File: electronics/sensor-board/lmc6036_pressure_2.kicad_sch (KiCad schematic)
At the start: 21 parts

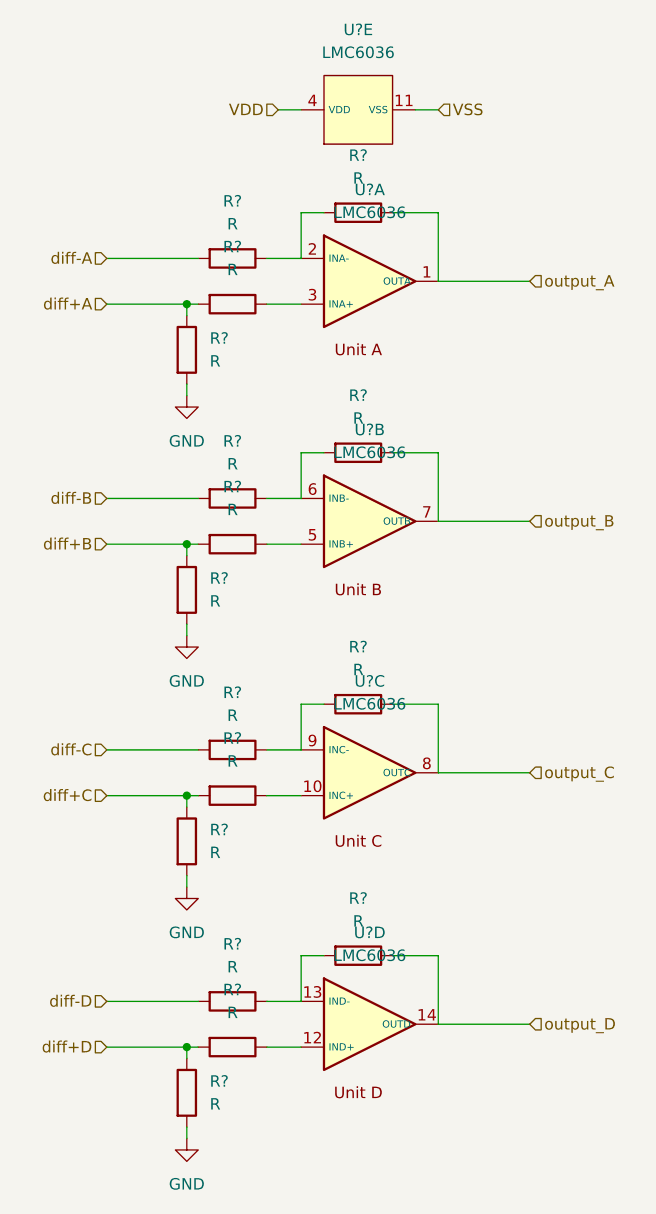
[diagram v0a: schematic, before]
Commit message: sensor-board edits
Finalized pressure and flow sensor circuits.
Reorganized schematics
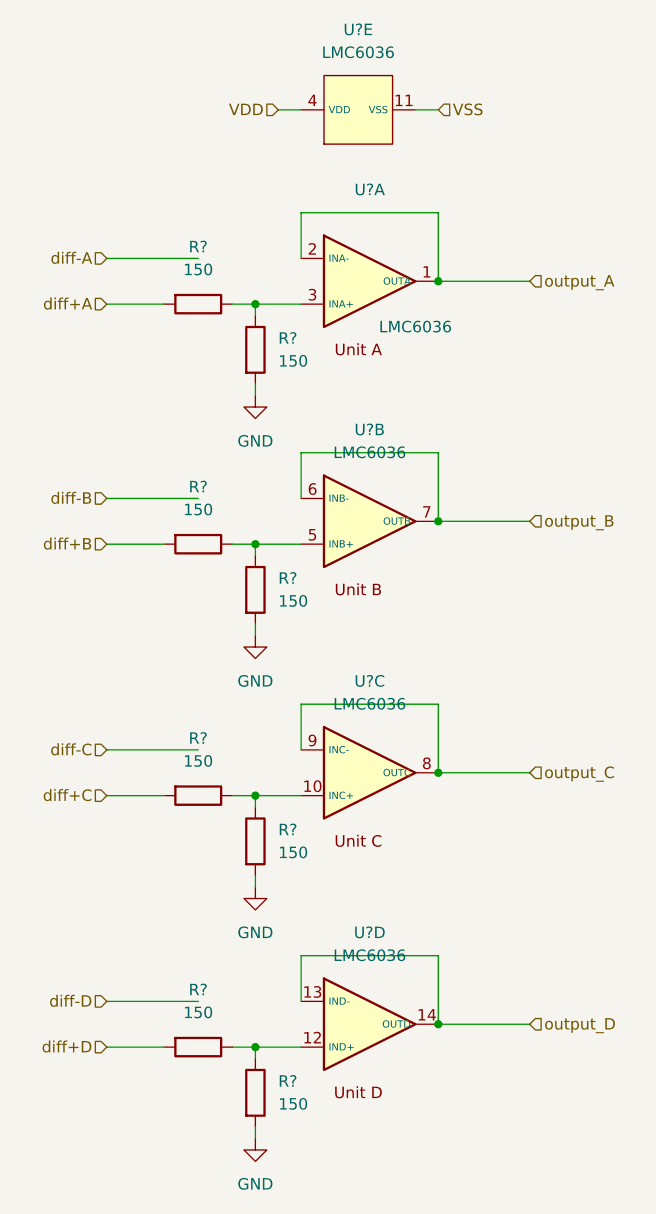
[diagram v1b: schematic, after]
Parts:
- removed R? (x16): R, symbol Device:R
- removed U? (x5): LMC6036, LMC6036:SOP65P640X120-14N, symbol LMC6036_custom:LMC6036
- added R? (x8): 150, symbol Device:R
- added U? (x5): LMC6036, LMC6036:SOP65P640X120-14N, symbol LMC6036_custom:LMC6036
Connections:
- net GND: now also R?.2, R?.2, R?.2, R?.2
- net VDD: now also U?.4 (VDD)
- net VSS: now also U?.11 (VSS)
- net diff+A: now also R?.2
- net diff+B: now also R?.2
- net diff+C: now also R?.2
- net diff+D: now also R?.2
- net output_A: now also U?.1 (OUTA), U?.2 (INA-)
- net output_B: now also U?.6 (INB-), U?.7 (OUTB)
- net output_C: now also U?.8 (OUTC), U?.9 (INC-)
- net output_D: now also U?.13 (IND-), U?.14 (OUTD)
- new net: R?.1, R?.1, U?.10 (INC+)
- new net: R?.1, R?.1, U?.3 (INA+)
- new net: R?.1, R?.1, U?.12 (IND+)
- new net: R?.1, R?.1, U?.5 (INB+)

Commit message: work on sensor-board
added MCP960 footprint
finished MCP960 array schematic
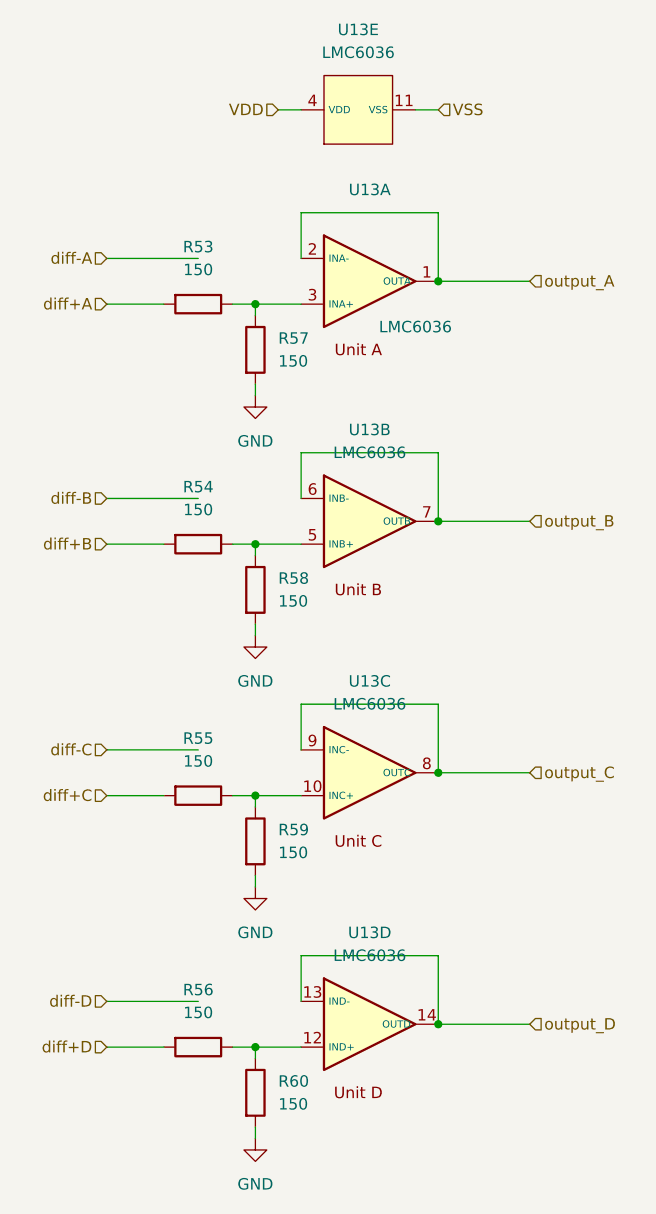
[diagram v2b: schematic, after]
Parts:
- R53, R54, R55, R56, R57, R58, R59, R60: renamed from R?; footprint (none) -> Resistor_SMD:R_0603_1608Metric
- gave numbers to parts that had none: 1
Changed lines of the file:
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@@
   (symbol (lib_id "power:GND") (at 142.24 76.2 0) (unit 1)
     (in_bom yes) (on_board yes) (fields_autoplaced)
-    (property "Reference" "#PWR?" (id 0) (at 142.24 82.55 0)
+    (property "Reference" "#PWR0181" (id 0) (at 142.24 82.55 0)
       (effects (font (size 1.27 1.27)) hide)
     )
@@
   (symbol (lib_id "power:GND") (at 142.24 102.87 0) (unit 1)
     (in_bom yes) (on_board yes) (fields_autoplaced)
-    (property "Reference" "#PWR?" (id 0) (at 142.24 109.22 0)
+    (property "Reference" "#PWR0183" (id 0) (at 142.24 109.22 0)
       (effects (font (size 1.27 1.27)) hide)
     )
@@
   (symbol (lib_id "power:GND") (at 142.24 130.81 0) (unit 1)
     (in_bom yes) (on_board yes) (fields_autoplaced)
-    (property "Reference" "#PWR?" (id 0) (at 142.24 137.16 0)
+    (property "Reference" "#PWR0182" (id 0) (at 142.24 137.16 0)
       (effects (font (size 1.27 1.27)) hide)
     )
@@
   (symbol (lib_id "power:GND") (at 142.24 158.75 0) (unit 1)
     (in_bom yes) (on_board yes) (fields_autoplaced)
-    (property "Reference" "#PWR?" (id 0) (at 142.24 165.1 0)
+    (property "Reference" "#PWR0184" (id 0) (at 142.24 165.1 0)
       (effects (font (size 1.27 1.27)) hide)
     )
@@
   (symbol (lib_id "Device:R") (at 135.89 66.04 270) (unit 1)
     (in_bom yes) (on_board yes) (fields_autoplaced)
-    (property "Reference" "R?" (id 0) (at 135.89 59.69 90))
+    (property "Reference" "R53" (id 0) (at 135.89 59.69 90))
     (property "Value" "150" (id 1) (at 135.89 62.23 90))
-    (property "Footprint" "" (id 2) (at 135.89 64.262 90)
+    (property "Footprint" "Resistor_SMD:R_0603_1608Metric" (id 2) (at 135.89 64.262 90)
       (effects (font (size 1.27 1.27)) hide)
     )
@@
   (symbol (lib_id "Device:R") (at 135.89 92.71 270) (unit 1)
     (in_bom yes) (on_board yes) (fields_autoplaced)
-    (property "Reference" "R?" (id 0) (at 135.89 86.36 90))
+    (property "Reference" "R54" (id 0) (at 135.89 86.36 90))
     (property "Value" "150" (id 1) (at 135.89 88.9 90))
-    (property "Footprint" "" (id 2) (at 135.89 90.932 90)
+    (property "Footprint" "Resistor_SMD:R_0603_1608Metric" (id 2) (at 135.89 90.932 90)
       (effects (font (size 1.27 1.27)) hide)
     )
@@
   (symbol (lib_id "Device:R") (at 135.89 120.65 270) (unit 1)
     (in_bom yes) (on_board yes) (fields_autoplaced)
-    (property "Reference" "R?" (id 0) (at 135.89 114.3 90))
+    (property "Reference" "R55" (id 0) (at 135.89 114.3 90))
     (property "Value" "150" (id 1) (at 135.89 116.84 90))
-    (property "Footprint" "" (id 2) (at 135.89 118.872 90)
+    (property "Footprint" "Resistor_SMD:R_0603_1608Metric" (id 2) (at 135.89 118.872 90)
       (effects (font (size 1.27 1.27)) hide)
     )
@@
   (symbol (lib_id "Device:R") (at 135.89 148.59 270) (unit 1)
     (in_bom yes) (on_board yes) (fields_autoplaced)
-    (property "Reference" "R?" (id 0) (at 135.89 142.24 90))
+    (property "Reference" "R56" (id 0) (at 135.89 142.24 90))
     (property "Value" "150" (id 1) (at 135.89 144.78 90))
-    (property "Footprint" "" (id 2) (at 135.89 146.812 90)
+    (property "Footprint" "Resistor_SMD:R_0603_1608Metric" (id 2) (at 135.89 146.812 90)
       (effects (font (size 1.27 1.27)) hide)
     )
@@
   (symbol (lib_id "Device:R") (at 142.24 71.12 0) (unit 1)
     (in_bom yes) (on_board yes) (fields_autoplaced)
-    (property "Reference" "R?" (id 0) (at 144.78 69.8499 0)
+    (property "Reference" "R57" (id 0) (at 144.78 69.8499 0)
       (effects (font (size 1.27 1.27)) (justify left))
     )
@@
       (effects (font (size 1.27 1.27)) (justify left))
     )
-    (property "Footprint" "" (id 2) (at 140.462 71.12 90)
+    (property "Footprint" "Resistor_SMD:R_0603_1608Metric" (id 2) (at 140.462 71.12 90)
       (effects (font (size 1.27 1.27)) hide)
     )
@@
   (symbol (lib_id "Device:R") (at 142.24 97.79 0) (unit 1)
     (in_bom yes) (on_board yes) (fields_autoplaced)
-    (property "Reference" "R?" (id 0) (at 144.78 96.5199 0)
+    (property "Reference" "R58" (id 0) (at 144.78 96.5199 0)
       (effects (font (size 1.27 1.27)) (justify left))
     )
@@
       (effects (font (size 1.27 1.27)) (justify left))
     )
-    (property "Footprint" "" (id 2) (at 140.462 97.79 90)
+    (property "Footprint" "Resistor_SMD:R_0603_1608Metric" (id 2) (at 140.462 97.79 90)
       (effects (font (size 1.27 1.27)) hide)
     )
@@
   (symbol (lib_id "Device:R") (at 142.24 125.73 0) (unit 1)
     (in_bom yes) (on_board yes) (fields_autoplaced)
-    (property "Reference" "R?" (id 0) (at 144.78 124.4599 0)
+    (property "Reference" "R59" (id 0) (at 144.78 124.4599 0)
       (effects (font (size 1.27 1.27)) (justify left))
     )
@@
       (effects (font (size 1.27 1.27)) (justify left))
     )
-    (property "Footprint" "" (id 2) (at 140.462 125.73 90)
+    (property "Footprint" "Resistor_SMD:R_0603_1608Metric" (id 2) (at 140.462 125.73 90)
       (effects (font (size 1.27 1.27)) hide)
     )
@@
   (symbol (lib_id "Device:R") (at 142.24 153.67 0) (unit 1)
     (in_bom yes) (on_board yes) (fields_autoplaced)
-    (property "Reference" "R?" (id 0) (at 144.78 152.3999 0)
+    (property "Reference" "R60" (id 0) (at 144.78 152.3999 0)
       (effects (font (size 1.27 1.27)) (justify left))
     )
@@
       (effects (font (size 1.27 1.27)) (justify left))
     )
-    (property "Footprint" "" (id 2) (at 140.462 153.67 90)
+    (property "Footprint" "Resistor_SMD:R_0603_1608Metric" (id 2) (at 140.462 153.67 90)
       (effects (font (size 1.27 1.27)) hide)
     )
@@
   (symbol (lib_id "LMC6036_custom:LMC6036") (at 153.67 44.45 90) (unit 5)
     (in_bom yes) (on_board yes) (fields_autoplaced)
-    (property "Reference" "U?" (id 0) (at 153.67 35.56 90))
+    (property "Reference" "U13" (id 0) (at 153.67 35.56 90))
     (property "Value" "LMC6036" (id 1) (at 153.67 38.1 90))
     (property "Footprint" "LMC6036:SOP65P640X120-14N" (id 2) (at 153.67 42.545 0)
@@
   (symbol (lib_id "LMC6036_custom:LMC6036") (at 153.67 63.5 0) (unit 1)
     (in_bom yes) (on_board yes)
-    (property "Reference" "U?" (id 0) (at 154.94 53.34 0))
+    (property "Reference" "U13" (id 0) (at 154.94 53.34 0))
     (property "Value" "LMC6036" (id 1) (at 160.02 68.58 0))
     (property "Footprint" "LMC6036:SOP65P640X120-14N" (id 2) (at 155.575 63.5 0)
@@
   (symbol (lib_id "LMC6036_custom:LMC6036") (at 153.67 90.17 0) (unit 2)
     (in_bom yes) (on_board yes) (fields_autoplaced)
-    (property "Reference" "U?" (id 0) (at 154.94 80.01 0))
+    (property "Reference" "U13" (id 0) (at 154.94 80.01 0))
     (property "Value" "LMC6036" (id 1) (at 154.94 82.55 0))
     (property "Footprint" "LMC6036:SOP65P640X120-14N" (id 2) (at 155.575 90.17 0)
@@
   (symbol (lib_id "LMC6036_custom:LMC6036") (at 153.67 118.11 0) (unit 3)
     (in_bom yes) (on_board yes) (fields_autoplaced)
-    (property "Reference" "U?" (id 0) (at 154.94 107.95 0))
+    (property "Reference" "U13" (id 0) (at 154.94 107.95 0))
     (property "Value" "LMC6036" (id 1) (at 154.94 110.49 0))
     (property "Footprint" "LMC6036:SOP65P640X120-14N" (id 2) (at 155.575 118.11 0)
@@
   (symbol (lib_id "LMC6036_custom:LMC6036") (at 153.67 146.05 0) (unit 4)
     (in_bom yes) (on_board yes) (fields_autoplaced)
-    (property "Reference" "U?" (id 0) (at 154.94 135.89 0))
+    (property "Reference" "U13" (id 0) (at 154.94 135.89 0))
     (property "Value" "LMC6036" (id 1) (at 154.94 138.43 0))
     (property "Footprint" "LMC6036:SOP65P640X120-14N" (id 2) (at 155.575 146.05 0)

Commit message: Finalized sensor-board schematic
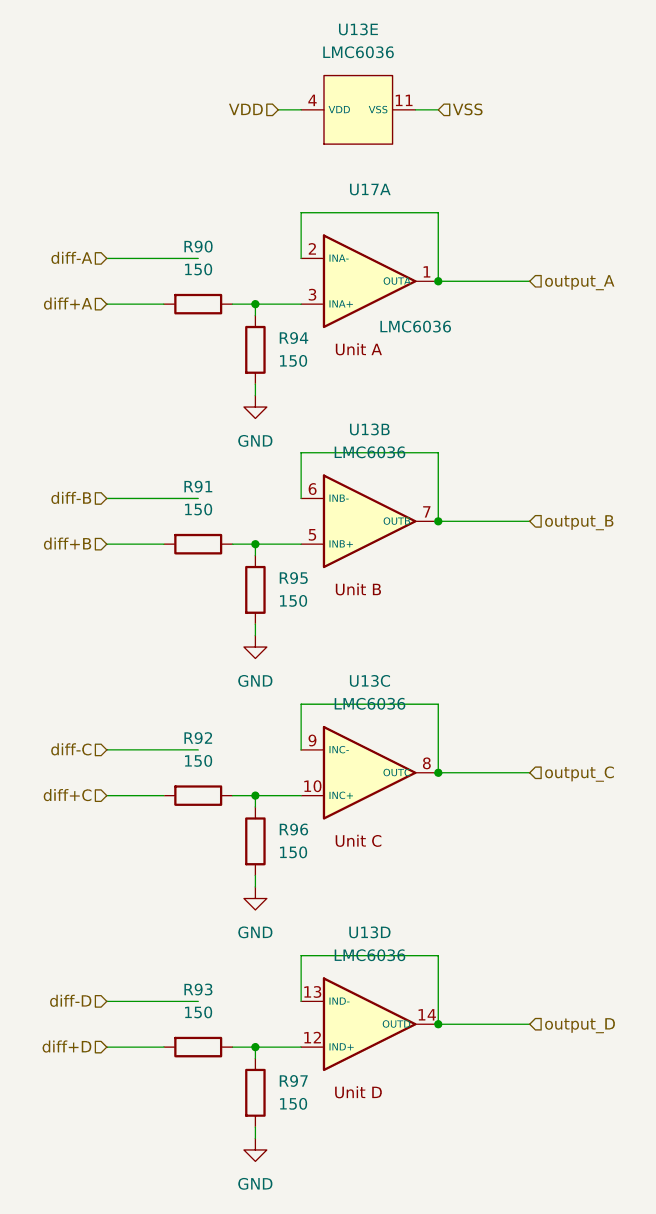
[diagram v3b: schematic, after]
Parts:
- renumbered R53 to R90, R54 to R91, R55 to R92, R56 to R93, R57 to R94, R58 to R95, R59 to R96, R60 to R97, U13 to U17
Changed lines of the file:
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@@
   (symbol (lib_id "power:GND") (at 142.24 76.2 0) (unit 1)
     (in_bom yes) (on_board yes) (fields_autoplaced)
-    (property "Reference" "#PWR0181" (id 0) (at 142.24 82.55 0)
+    (property "Reference" "#PWR0127" (id 0) (at 142.24 82.55 0)
       (effects (font (size 1.27 1.27)) hide)
     )
@@
   (symbol (lib_id "power:GND") (at 142.24 102.87 0) (unit 1)
     (in_bom yes) (on_board yes) (fields_autoplaced)
-    (property "Reference" "#PWR0183" (id 0) (at 142.24 109.22 0)
+    (property "Reference" "#PWR0128" (id 0) (at 142.24 109.22 0)
       (effects (font (size 1.27 1.27)) hide)
     )
@@
   (symbol (lib_id "power:GND") (at 142.24 130.81 0) (unit 1)
     (in_bom yes) (on_board yes) (fields_autoplaced)
-    (property "Reference" "#PWR0182" (id 0) (at 142.24 137.16 0)
+    (property "Reference" "#PWR0129" (id 0) (at 142.24 137.16 0)
       (effects (font (size 1.27 1.27)) hide)
     )
@@
   (symbol (lib_id "power:GND") (at 142.24 158.75 0) (unit 1)
     (in_bom yes) (on_board yes) (fields_autoplaced)
-    (property "Reference" "#PWR0184" (id 0) (at 142.24 165.1 0)
+    (property "Reference" "#PWR0130" (id 0) (at 142.24 165.1 0)
       (effects (font (size 1.27 1.27)) hide)
     )
@@
   (symbol (lib_id "Device:R") (at 135.89 66.04 270) (unit 1)
     (in_bom yes) (on_board yes) (fields_autoplaced)
-    (property "Reference" "R53" (id 0) (at 135.89 59.69 90))
+    (property "Reference" "R90" (id 0) (at 135.89 59.69 90))
     (property "Value" "150" (id 1) (at 135.89 62.23 90))
     (property "Footprint" "Resistor_SMD:R_0603_1608Metric" (id 2) (at 135.89 64.262 90)
@@
   (symbol (lib_id "Device:R") (at 135.89 92.71 270) (unit 1)
     (in_bom yes) (on_board yes) (fields_autoplaced)
-    (property "Reference" "R54" (id 0) (at 135.89 86.36 90))
+    (property "Reference" "R91" (id 0) (at 135.89 86.36 90))
     (property "Value" "150" (id 1) (at 135.89 88.9 90))
     (property "Footprint" "Resistor_SMD:R_0603_1608Metric" (id 2) (at 135.89 90.932 90)
@@
   (symbol (lib_id "Device:R") (at 135.89 120.65 270) (unit 1)
     (in_bom yes) (on_board yes) (fields_autoplaced)
-    (property "Reference" "R55" (id 0) (at 135.89 114.3 90))
+    (property "Reference" "R92" (id 0) (at 135.89 114.3 90))
     (property "Value" "150" (id 1) (at 135.89 116.84 90))
     (property "Footprint" "Resistor_SMD:R_0603_1608Metric" (id 2) (at 135.89 118.872 90)
@@
   (symbol (lib_id "Device:R") (at 135.89 148.59 270) (unit 1)
     (in_bom yes) (on_board yes) (fields_autoplaced)
-    (property "Reference" "R56" (id 0) (at 135.89 142.24 90))
+    (property "Reference" "R93" (id 0) (at 135.89 142.24 90))
     (property "Value" "150" (id 1) (at 135.89 144.78 90))
     (property "Footprint" "Resistor_SMD:R_0603_1608Metric" (id 2) (at 135.89 146.812 90)
@@
   (symbol (lib_id "Device:R") (at 142.24 71.12 0) (unit 1)
     (in_bom yes) (on_board yes) (fields_autoplaced)
-    (property "Reference" "R57" (id 0) (at 144.78 69.8499 0)
+    (property "Reference" "R94" (id 0) (at 144.78 69.8499 0)
       (effects (font (size 1.27 1.27)) (justify left))
     )
@@
   (symbol (lib_id "Device:R") (at 142.24 97.79 0) (unit 1)
     (in_bom yes) (on_board yes) (fields_autoplaced)
-    (property "Reference" "R58" (id 0) (at 144.78 96.5199 0)
+    (property "Reference" "R95" (id 0) (at 144.78 96.5199 0)
       (effects (font (size 1.27 1.27)) (justify left))
     )
@@
   (symbol (lib_id "Device:R") (at 142.24 125.73 0) (unit 1)
     (in_bom yes) (on_board yes) (fields_autoplaced)
-    (property "Reference" "R59" (id 0) (at 144.78 124.4599 0)
+    (property "Reference" "R96" (id 0) (at 144.78 124.4599 0)
       (effects (font (size 1.27 1.27)) (justify left))
     )
@@
   (symbol (lib_id "Device:R") (at 142.24 153.67 0) (unit 1)
     (in_bom yes) (on_board yes) (fields_autoplaced)
-    (property "Reference" "R60" (id 0) (at 144.78 152.3999 0)
+    (property "Reference" "R97" (id 0) (at 144.78 152.3999 0)
       (effects (font (size 1.27 1.27)) (justify left))
     )
@@
   (symbol (lib_id "LMC6036_custom:LMC6036") (at 153.67 63.5 0) (unit 1)
     (in_bom yes) (on_board yes)
-    (property "Reference" "U13" (id 0) (at 154.94 53.34 0))
+    (property "Reference" "U17" (id 0) (at 154.94 53.34 0))
     (property "Value" "LMC6036" (id 1) (at 160.02 68.58 0))
     (property "Footprint" "LMC6036:SOP65P640X120-14N" (id 2) (at 155.575 63.5 0)
